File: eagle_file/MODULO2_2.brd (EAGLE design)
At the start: 129.5 x 90.2 mm, 58 parts, among them IC1 74HC595N

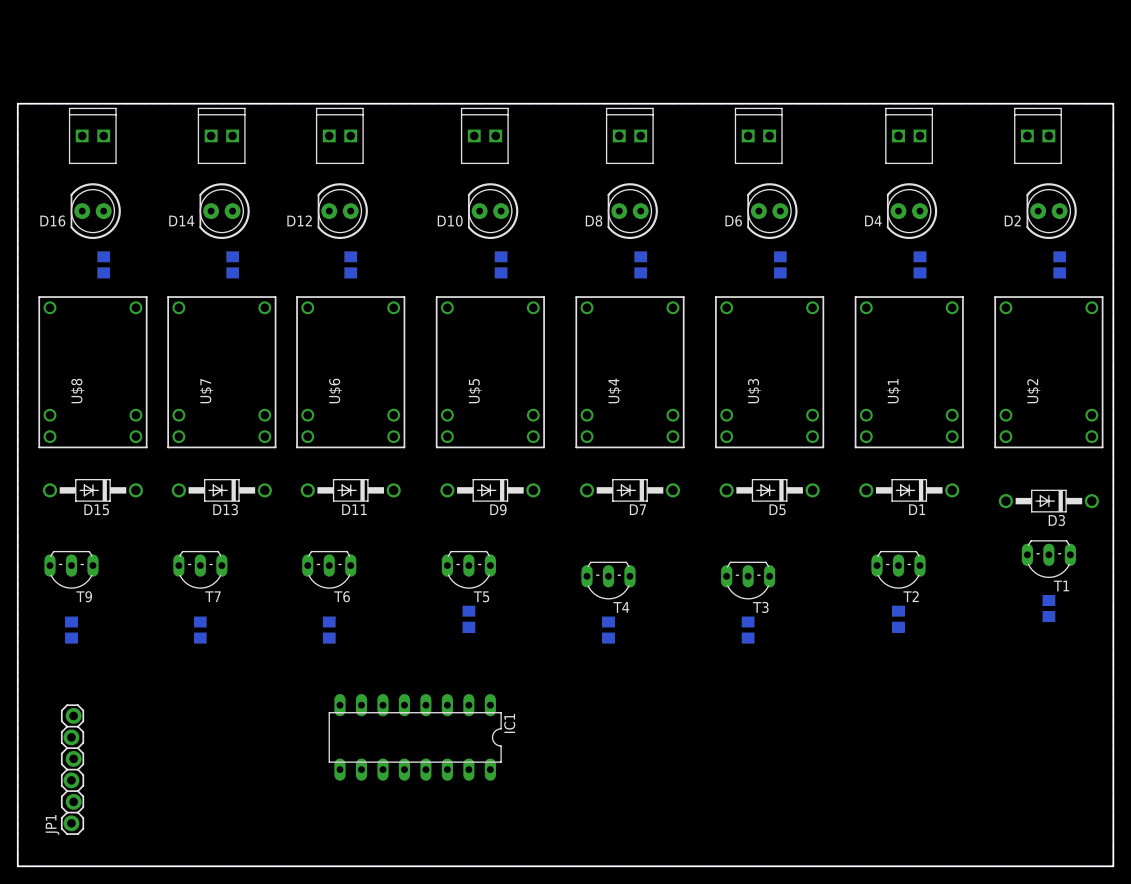
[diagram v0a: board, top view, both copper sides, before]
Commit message: Modulo 2_1
Modolo2_1.pdf per controllare i footprint
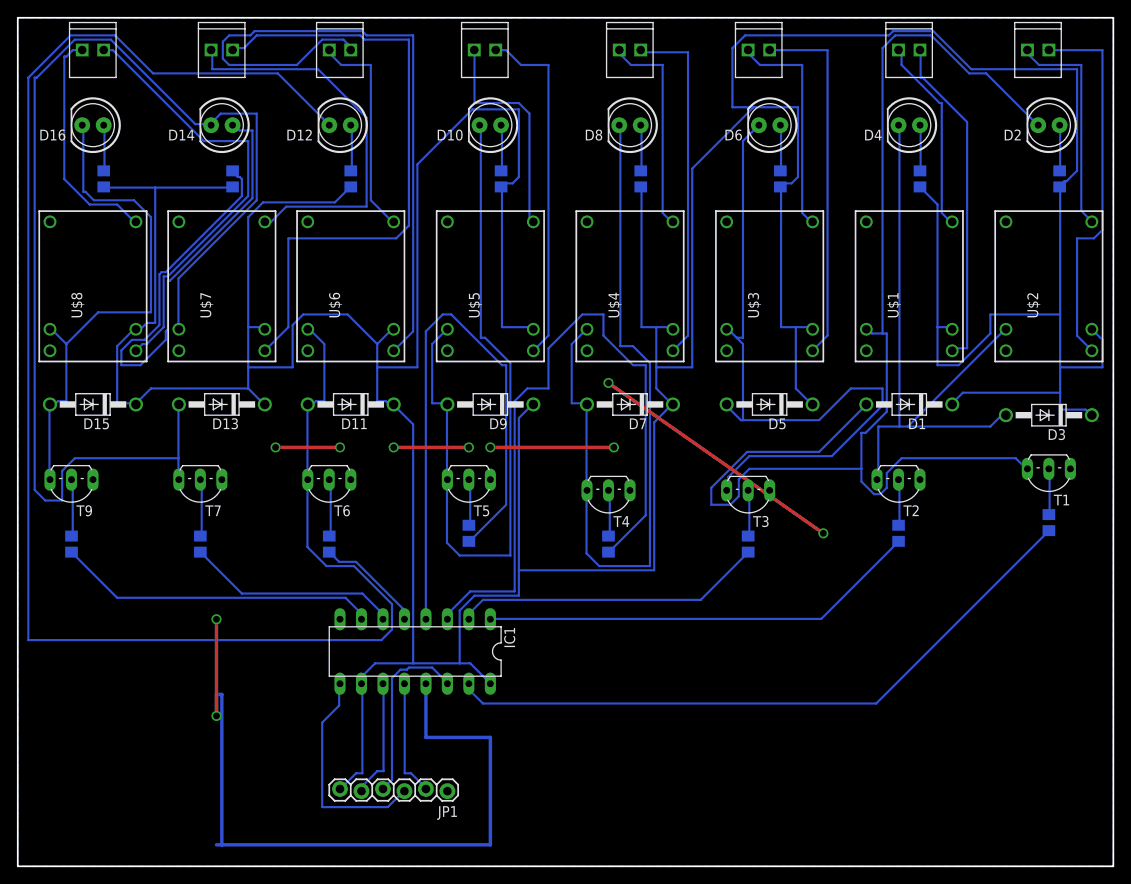
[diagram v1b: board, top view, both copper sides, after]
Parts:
- moved JP1 44.6 mm to (50.8, 8.89), turned to 180 degrees
- moved D3 10.2 mm to (121.9, 53.3)
- moved T2 10.2 mm to (104.1, 44.5)
- moved T5 10.2 mm to (53.3, 44.5)
- moved T6 10.2 mm to (36.8, 44.5)
- moved T7 10.2 mm to (21.6, 44.5)
- moved T9 10.2 mm to (6.35, 44.5)
- moved R1 10.2 mm to (121.9, 40.6)
- moved R11 10.2 mm to (36.8, 38.1)
- moved R13 10.2 mm to (21.6, 38.1)
- moved R15 10.2 mm to (6.35, 38.1)
- moved R5 10.2 mm to (86.4, 38.1)
- moved R7 10.2 mm to (69.8, 38.1)
- moved IC1 10.2 mm to (47.0, 25.4)
- moved D1 10.2 mm to (105.4, 54.6)
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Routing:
- net VCC: track 0.00 -> 622.9 mm
- net N$20: track 0.00 -> 196.3 mm
- net GND: track 0.00 -> 153.6 mm, vias 0 -> 10
- net N$3: track 0.00 -> 147.5 mm
- net N$23: track 0.00 -> 141.6 mm
- net N$10: track 0.00 -> 91.7 mm
- net N$17: track 0.00 -> 88.6 mm
- net N$7: track 0.00 -> 84.7 mm
- net N$13: track 0.00 -> 82.7 mm
- net N$44: track 0.00 -> 81.0 mm
- net N$1: track 0.00 -> 78.4 mm
- net N$6: track 0.00 -> 74.1 mm
- net N$46: track 0.00 -> 73.1 mm
- net N$30: track 0.00 -> 69.5 mm
- net N$24: track 0.00 -> 68.9 mm
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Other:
- board size 129.5 x 90.2 mm -> 129.5 x 100.3 mm
